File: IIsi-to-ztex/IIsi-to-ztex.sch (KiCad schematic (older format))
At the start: 2 parts

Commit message: cleanup DRC
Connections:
- no-connect marks 0 -> 2
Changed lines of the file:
@@
 F1 "pmod.sch" 50
 $EndSheet
+NoConn ~ 5775 1525
+NoConn ~ 5775 1250
 $EndSCHEMATC

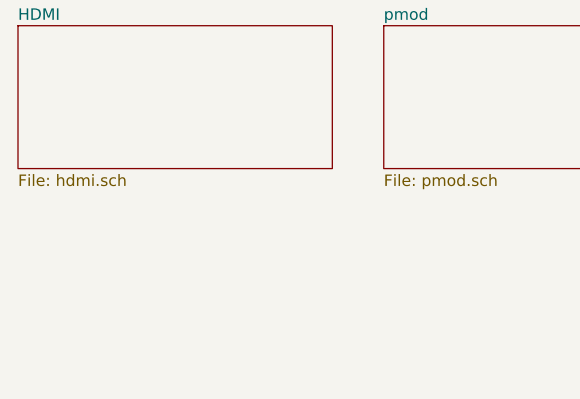
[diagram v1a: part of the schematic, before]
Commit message: 3V3 SRAM draft
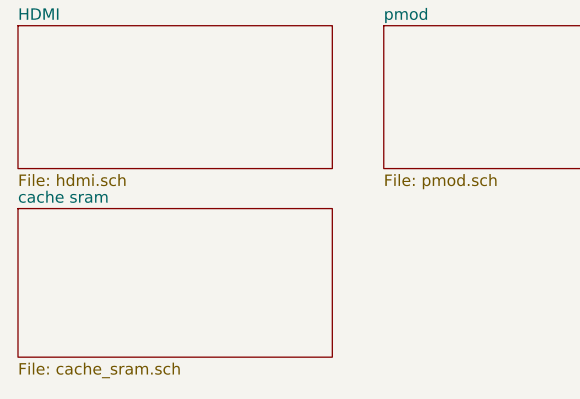
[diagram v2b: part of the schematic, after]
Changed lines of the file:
@@
 $Descr A4 11693 8268
 encoding utf-8
-Sheet 1 5
+Sheet 1 6
 Title ""
 Date ""
@@
 NoConn ~ 5775 1525
 NoConn ~ 5775 1250
+$Sheet
+S 1025 2725 1375 650
+U 64849023
+F0 "cache sram" 50
+F1 "cache_sram.sch" 50
+$EndSheet
 $EndSCHEMATC
